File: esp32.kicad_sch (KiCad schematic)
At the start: 21 parts, among them J2 TC2030-IDC, J3 Conn_01x04, J4 Conn_01x06, J5 USB_C_Receptacle_USB2.0, SW1 GT-TC029B-H025-L1N, SW2 GT-TC029B-H025-L1N, U3 RT9080-33GJ5, U4 ESP32-S3-WROOM-1

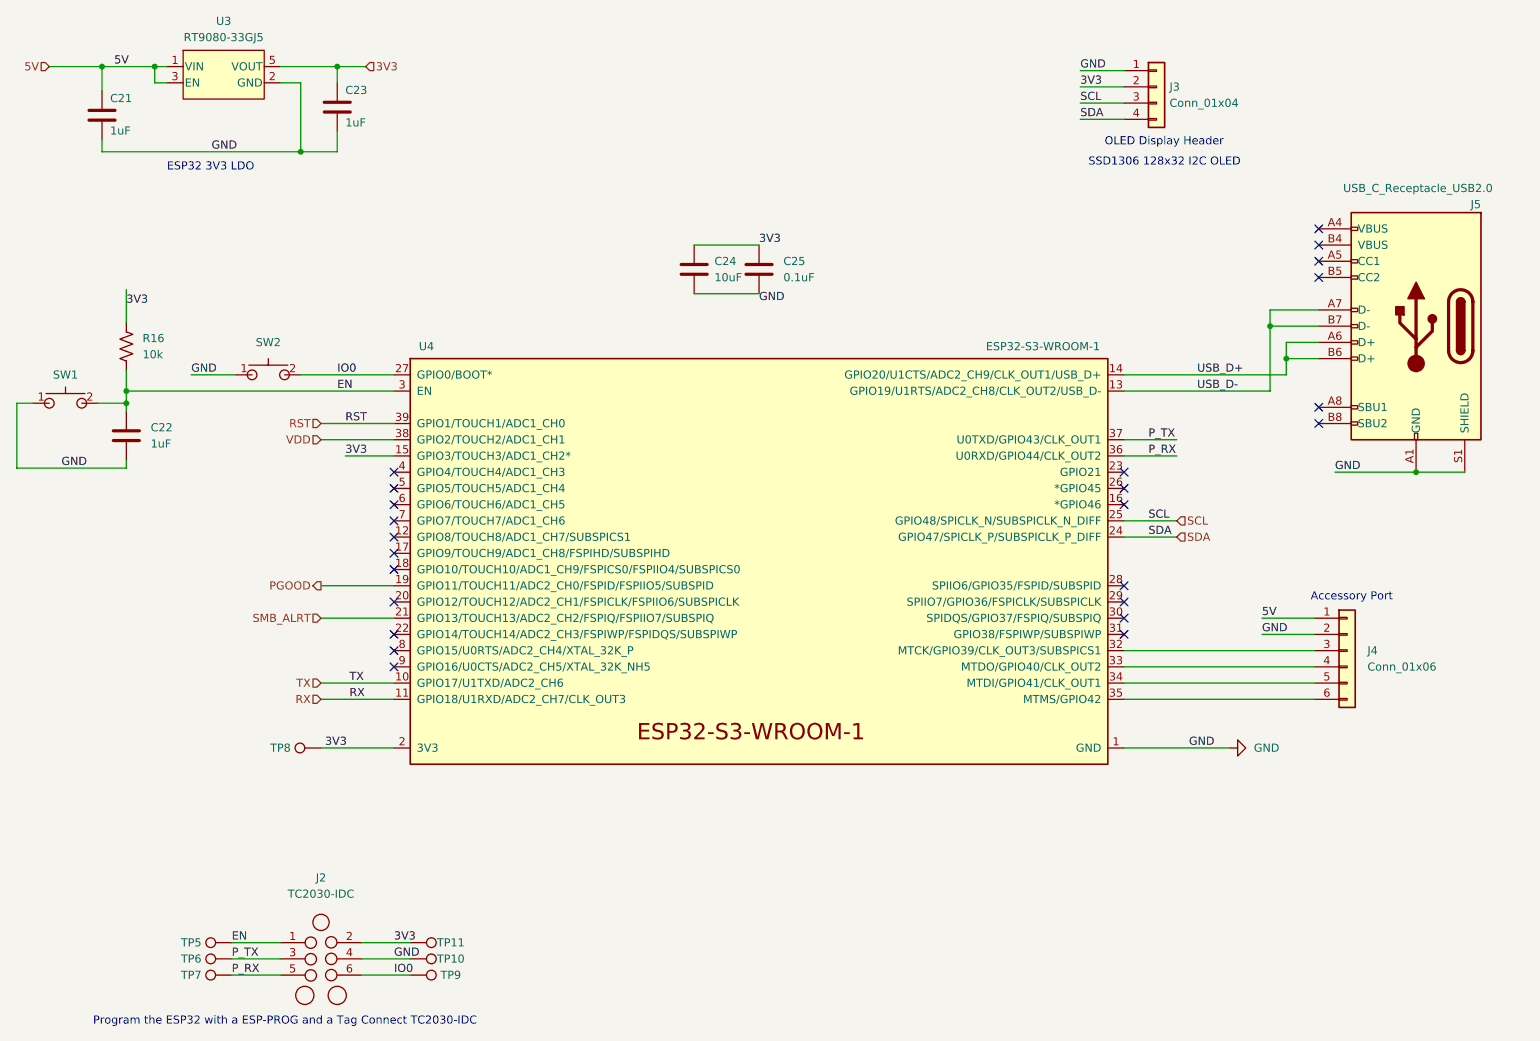
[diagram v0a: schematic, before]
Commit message: fix off-grid and unconnected erc warnings
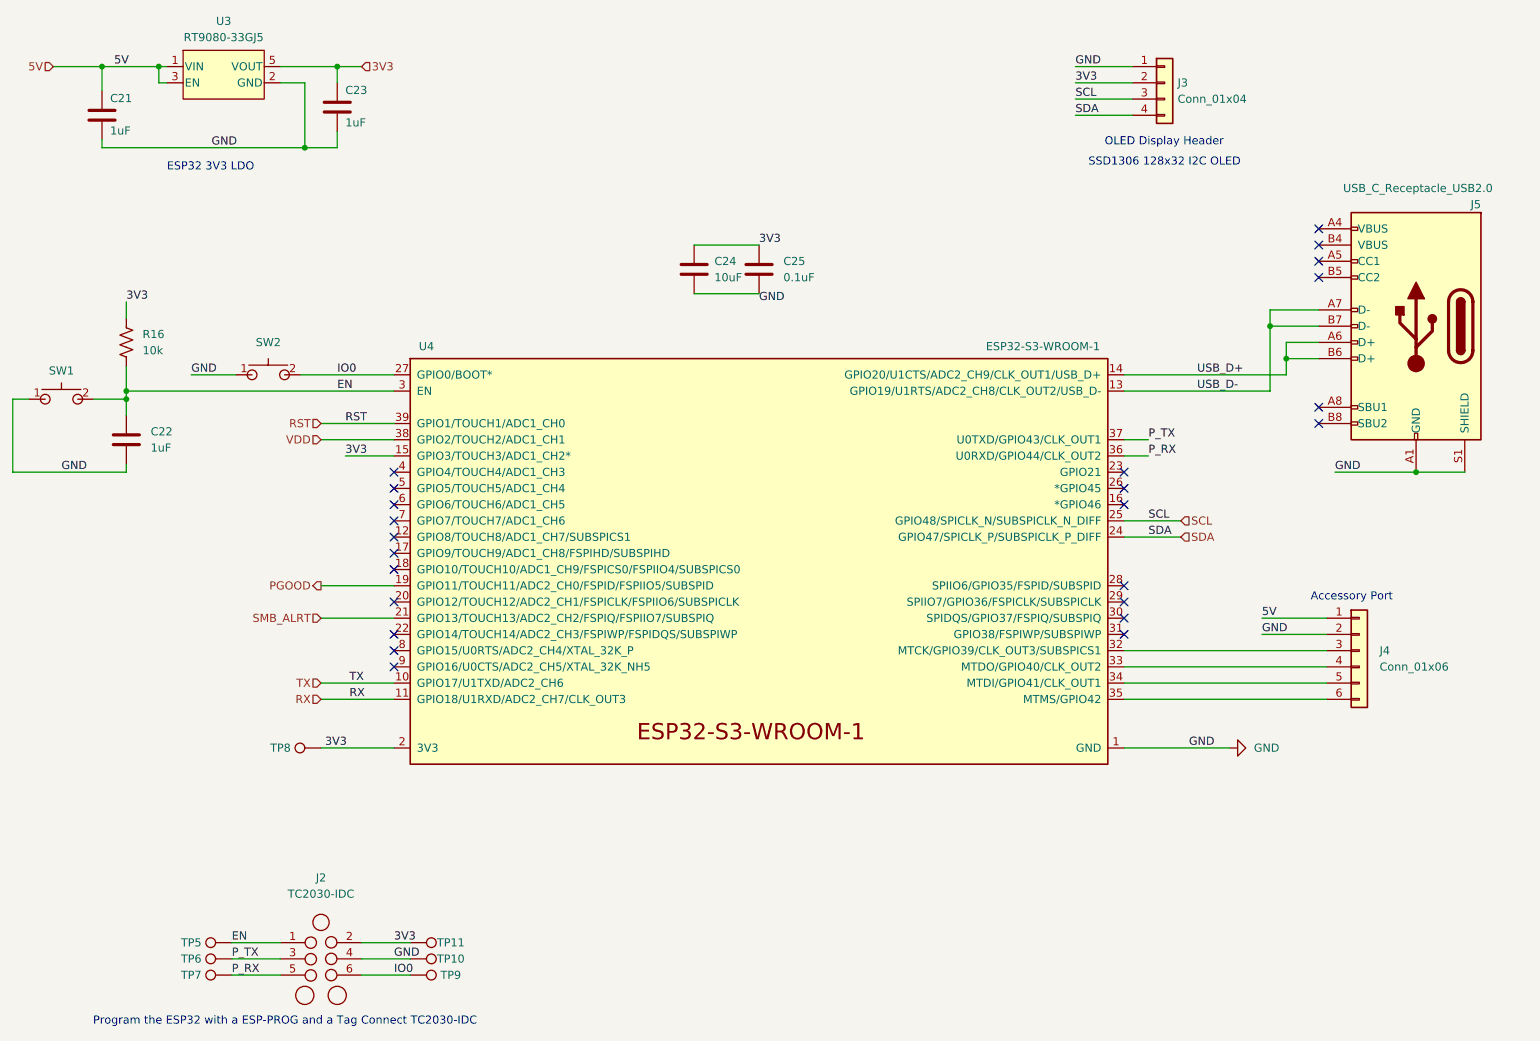
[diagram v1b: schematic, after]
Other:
- moved on the sheet: C22, J3, J4, R16, SW1
